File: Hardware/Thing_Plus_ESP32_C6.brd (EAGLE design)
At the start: 22.9 x 58.4 mm, 125 parts, among them J1 THING_PLUS_LOGICAL, J4 QWIIC_RIGHT_ANGLE, J5 MICRO-SDFRICTION, Q1 20V/4.2A/52mΩ/1.4W, Q2 20V/4.2A/52mΩ/1.4W, U1 ESP32-C6-WROOM-1-NARROW, U2 RT9080-33GJ5, U3 MCP73831, U4 MAX17048

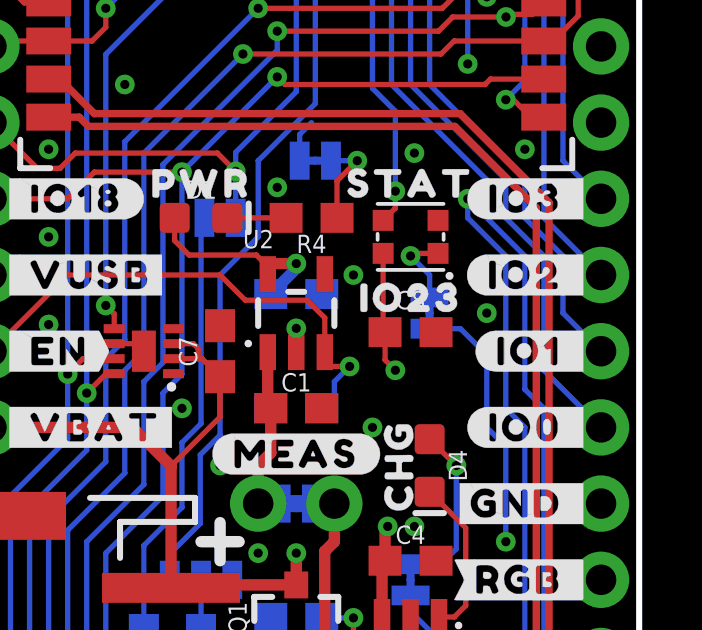
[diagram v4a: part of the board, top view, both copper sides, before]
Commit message: Change RGB jumper to NO
Won't violate the form factor standard by default this time!
Also update panel files
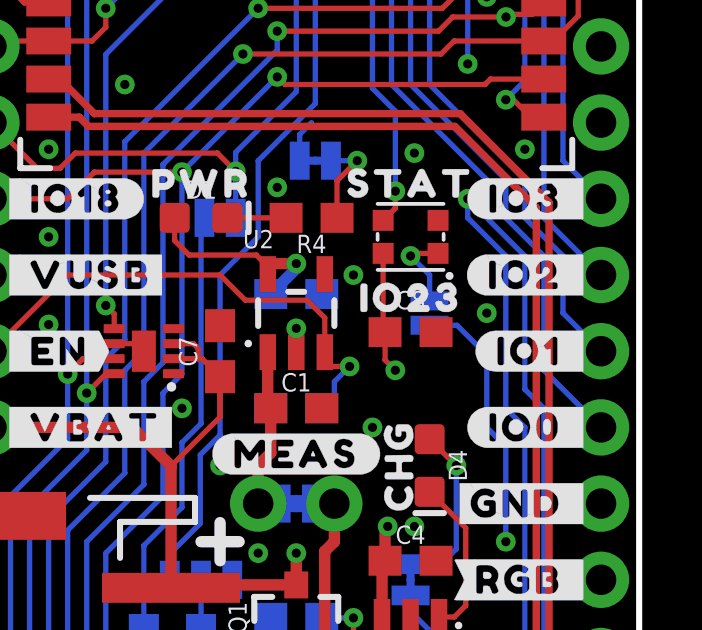
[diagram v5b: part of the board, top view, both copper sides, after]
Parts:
- RGB: value JUMPER-SMT_2_NC_TRACE_SILK -> JUMPER-SMT_2_NO_SILK; device SparkFun-Jumpers:SMT-JUMPER_2_NC_TRACE_SILK -> SparkFun-Jumpers:SMT-JUMPER_2_NO_SILK
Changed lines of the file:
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@@
 <drawing>
 <settings>
-<setting alwaysvectorfont="no"/>
+<setting alwaysvectorfont="yes"/>
 <setting verticaltext="up"/>
 </settings>
@@
 <layers>
 <layer number="1" name="Top" color="4" fill="1" visible="yes" active="yes"/>
-<layer number="2" name="Route2" color="23" fill="1" visible="no" active="yes"/>
-<layer number="15" name="Route15" color="11" fill="1" visible="no" active="yes"/>
+<layer number="2" name="Route2" color="23" fill="1" visible="yes" active="yes"/>
+<layer number="15" name="Route15" color="11" fill="1" visible="yes" active="yes"/>
 <layer number="16" name="Bottom" color="1" fill="1" visible="yes" active="yes"/>
 <layer number="17" name="Pads" color="2" fill="1" visible="yes" active="yes"/>
@@
 <element name="U$54" library="output" package="CHG0" value="" x="14.859" y="22.86" smashed="yes" rot="R90"/>
 <element name="U$55" library="output" package="STAT0" value="" x="15.24" y="32.258" smashed="yes"/>
-<element name="RGB" library="SparkFun-Jumpers" package="SMT-JUMPER_2_NC_TRACE_SILK" package3d_urn="urn:adsk.eagle:package:39281/1" value="JUMPER-SMT_2_NC_TRACE_SILK" x="15.875" y="27.94" smashed="yes" rot="MR90">
+<element name="RGB" library="SparkFun-Jumpers" package="SMT-JUMPER_2_NO_SILK" package3d_urn="urn:adsk.eagle:package:39279/1" value="JUMPER-SMT_2_NO_SILK" x="15.875" y="27.94" smashed="yes" rot="MR90">
 <attribute name="NAME" x="17.018" y="27.94" size="0.6096" layer="26" font="vector" ratio="20" rot="MR90" align="bottom-center"/>
 <attribute name="VALUE" x="14.732" y="27.94" size="0.6096" layer="28" font="vector" ratio="20" rot="MR90" align="top-center"/>
@@
 <wire x1="19.05" y1="19.05" x2="21.59" y2="19.05" width="0.1778" layer="15"/>
 <wire x1="19.05" y1="19.05" x2="18.415" y2="19.685" width="0.1778" layer="15"/>
-<wire x1="16.9037" y1="27.4193" x2="15.875" y2="27.4193" width="0.1778" layer="16"/>
-<wire x1="17.78" y1="26.543" x2="16.9037" y2="27.4193" width="0.1778" layer="16"/>
+<wire x1="16.7894" y1="27.5336" x2="15.875" y2="27.5336" width="0.1778" layer="16"/>
+<wire x1="17.78" y1="26.543" x2="16.7894" y2="27.5336" width="0.1778" layer="16"/>
 </signal>
 <signal name="N$14">
@@
 <via x="15.24" y="29.845" extent="1-16" drill="0.3048"/>
 <wire x1="15.24" y1="29.845" x2="15.875" y2="29.21" width="0.1778" layer="16"/>
-<wire x1="15.875" y1="29.21" x2="15.875" y2="28.4607" width="0.1778" layer="16"/>
+<wire x1="15.875" y1="29.21" x2="15.875" y2="28.3464" width="0.1778" layer="16"/>
 </signal>
 <signal name="N$16">

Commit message: Change C6 to DNP
Rise time was slow, causing chip to run bootloader instead of booting from flash
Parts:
- C6: value 0.1uF -> DNP
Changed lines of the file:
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@@
 <attribute name="VALUE" x="19.431" y="10.722" size="0.6096" layer="28" font="vector" ratio="20" rot="MR180" align="top-center"/>
 </element>
-<element name="C6" library="SparkFun-Capacitors" package="0603" value="0.1uF" x="19.431" y="8.255" smashed="yes" rot="MR0">
+<element name="C6" library="SparkFun-Capacitors" package="0603" value="DNP" x="19.431" y="8.255" smashed="yes" rot="MR0">
 <attribute name="NAME" x="19.431" y="8.817" size="0.6096" layer="26" font="vector" ratio="20" rot="MR0" align="bottom-center"/>
-<attribute name="PROD_ID" value="CAP-00810" x="35.941" y="0.635" size="1.778" layer="28" font="vector" ratio="15" rot="MR0" display="off"/>
+<attribute name="PROD_ID" value="" x="35.941" y="0.635" size="1.778" layer="28" font="vector" ratio="15" rot="MR0" display="off"/>
 <attribute name="VALUE" x="19.431" y="7.693" size="0.6096" layer="28" font="vector" ratio="20" rot="MR0" align="top-center"/>
 </element>
